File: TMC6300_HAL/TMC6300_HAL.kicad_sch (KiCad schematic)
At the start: 31 parts, among them IC101 STM32L431KBU6, J101 B8B-PH-K-S_LF__SN_, J102 B3B-PH-K-S_LF__SN_, J103 B2B-PH-K-S_LF__SN_, J104 20021121-00006T4LF

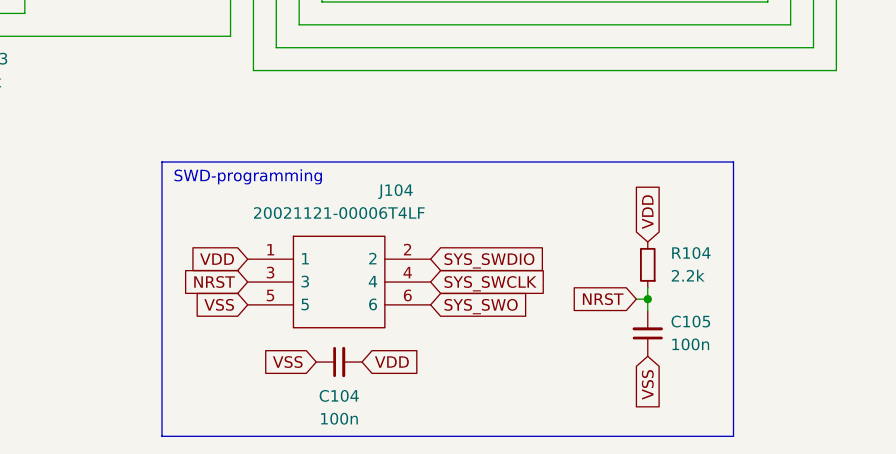
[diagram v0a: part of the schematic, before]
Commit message: Version used with Lencon blower.
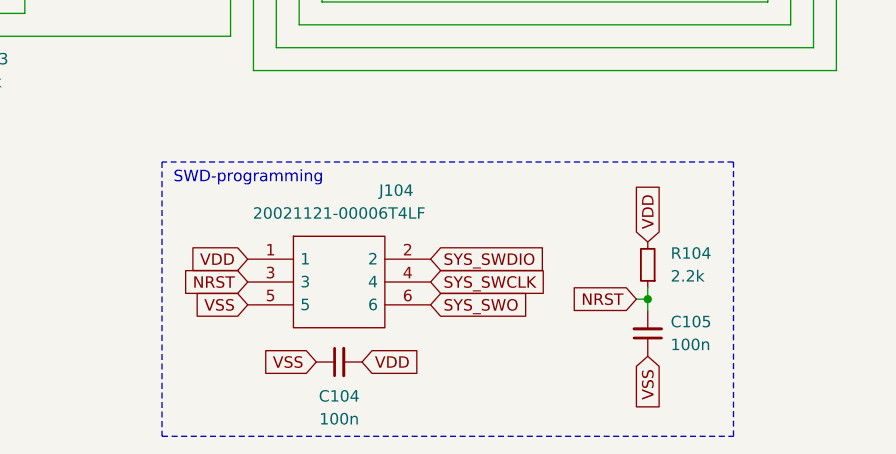
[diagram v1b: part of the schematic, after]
